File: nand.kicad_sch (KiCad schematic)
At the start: 14 parts, among them U4 MCIMX6Y2DVM09AB, U7 MT29F4G08ABAEAH4

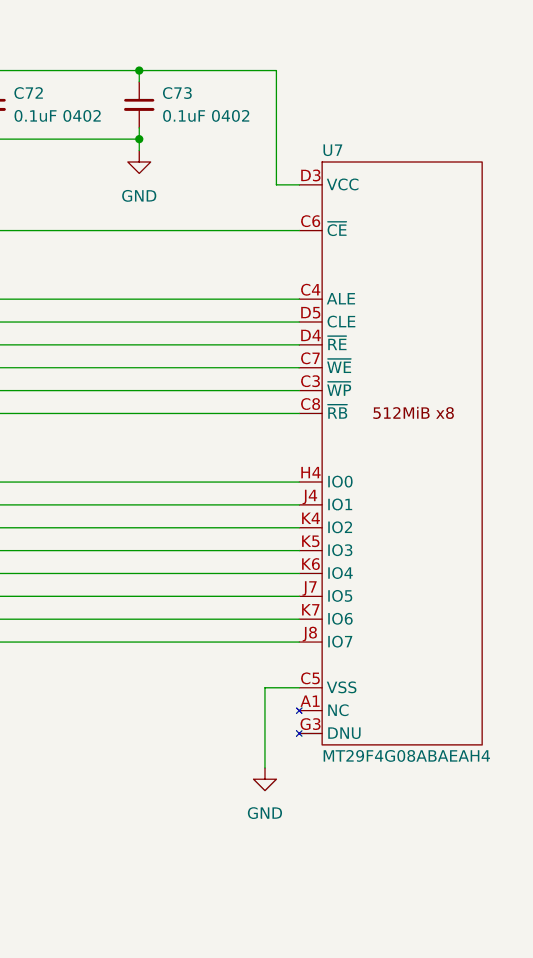
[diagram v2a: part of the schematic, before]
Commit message: Fix NAND and RClamp3374N footprints; ERC
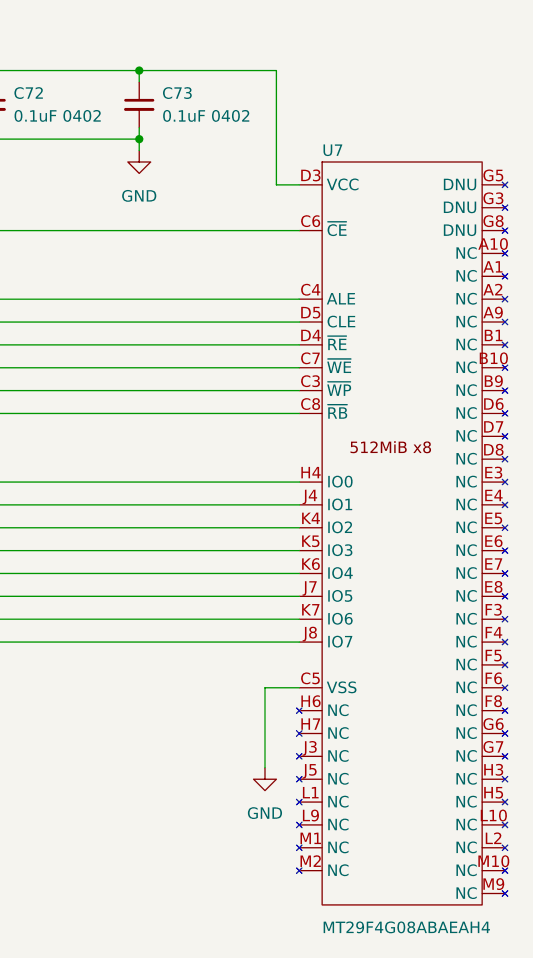
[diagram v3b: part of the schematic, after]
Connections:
- net VCC renamed VDD_3V3
- now unconnected: U7.A1 (NC), U7.A10 (NC), U7.A2 (NC), U7.A9 (NC), U7.B1 (NC), U7.B10 (NC), U7.B9 (NC), U7.D6 (NC), U7.D7 (NC), U7.D8 (NC), U7.E3 (NC), U7.E4 (NC), U7.E5 (NC), U7.E6 (NC), U7.E7 (NC), U7.E8 (NC), U7.F3 (NC), U7.F4 (NC), U7.F5 (NC), U7.F6 (NC), U7.F8 (NC), U7.G3 (DNU), U7.G5 (DNU), U7.G6 (NC), U7.G7 (NC), U7.G8 (DNU), U7.H3 (NC), U7.H5 (NC), U7.H6 (NC), U7.H7 (NC), U7.J3 (NC), U7.J5 (NC), U7.L1 (NC), U7.L10 (NC), U7.L2 (NC), U7.L9 (NC), U7.M1 (NC), U7.M10 (NC), U7.M2 (NC), U7.M9 (NC)
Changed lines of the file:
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@@
       (effects (font (size 1.27 1.27)) (justify left))
     )
-    (property "Value" "MT29F4G08ABAEAH4" (id 1) (at 230.505 135.255 0)
+    (property "Value" "MT29F4G08ABAEAH4" (id 1) (at 230.505 154.305 0)
       (effects (font (size 1.27 1.27)) (justify left))
     )

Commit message: Footprint assignments for standard passives
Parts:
- C67, C68, C70, C71, C72, C73: footprint (none) -> Capacitor_SMD:C_0402_1005Metric
- C69: footprint (none) -> Capacitor_SMD:C_0603_1608Metric
- R22, R23, R24, R25, R26: footprint (none) -> Resistor_SMD:R_0402_1005Metric
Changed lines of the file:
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@@
       (effects (font (size 1.27 1.27)) (justify left))
     )
-    (property "Footprint" "" (id 2) (at 113.665 133.985 0)
+    (property "Footprint" "Capacitor_SMD:C_0402_1005Metric" (id 2) (at 113.665 133.985 0)
       (effects (font (size 1.27 1.27)) hide)
     )
@@
       (effects (font (size 1.27 1.27)) (justify left))
     )
-    (property "Footprint" "" (id 2) (at 210.185 62.865 0)
+    (property "Footprint" "Capacitor_SMD:C_0402_1005Metric" (id 2) (at 210.185 62.865 0)
       (effects (font (size 1.27 1.27)) hide)
     )
@@
       (effects (font (size 1.27 1.27)) (justify left))
     )
-    (property "Footprint" "" (id 2) (at 27.94 81.915 0)
+    (property "Footprint" "Capacitor_SMD:C_0402_1005Metric" (id 2) (at 27.94 81.915 0)
       (effects (font (size 1.27 1.27)) hide)
     )
@@
       (effects (font (size 1.27 1.27)) (justify left))
     )
-    (property "Footprint" "" (id 2) (at 193.675 62.865 0)
+    (property "Footprint" "Capacitor_SMD:C_0402_1005Metric" (id 2) (at 193.675 62.865 0)
       (effects (font (size 1.27 1.27)) hide)
     )
@@
       (effects (font (size 1.27 1.27)) (justify left))
     )
-    (property "Footprint" "" (id 2) (at 118.745 71.755 0)
+    (property "Footprint" "Resistor_SMD:R_0402_1005Metric" (id 2) (at 118.745 71.755 0)
       (effects (font (size 1.27 1.27)) hide)
     )
@@
       (effects (font (size 1.27 1.27)) (justify left))
     )
-    (property "Footprint" "" (id 2) (at 144.145 62.865 0)
+    (property "Footprint" "Capacitor_SMD:C_0603_1608Metric" (id 2) (at 144.145 62.865 0)
       (effects (font (size 1.27 1.27)) hide)
     )
@@
       (effects (font (size 0.8 0.8)))
     )
-    (property "Footprint" "" (id 2) (at 94.615 92.075 0)
+    (property "Footprint" "Resistor_SMD:R_0402_1005Metric" (id 2) (at 94.615 92.075 0)
       (effects (font (size 1.27 1.27)) hide)
     )
@@
       (effects (font (size 0.8 0.8)))
     )
-    (property "Footprint" "" (id 2) (at 94.615 89.535 0)
+    (property "Footprint" "Resistor_SMD:R_0402_1005Metric" (id 2) (at 94.615 89.535 0)
       (effects (font (size 1.27 1.27)) hide)
     )
@@
       (effects (font (size 1.27 1.27)) (justify left))
     )
-    (property "Footprint" "" (id 2) (at 177.165 62.865 0)
+    (property "Footprint" "Capacitor_SMD:C_0402_1005Metric" (id 2) (at 177.165 62.865 0)
       (effects (font (size 1.27 1.27)) hide)
     )
@@
       (effects (font (size 1.27 1.27)) (justify left))
     )
-    (property "Footprint" "" (id 2) (at 160.655 62.865 0)
+    (property "Footprint" "Capacitor_SMD:C_0402_1005Metric" (id 2) (at 160.655 62.865 0)
       (effects (font (size 1.27 1.27)) hide)
     )
@@
       (effects (font (size 1.27 1.27)) (justify left))
     )
-    (property "Footprint" "" (id 2) (at 104.775 71.755 0)
+    (property "Footprint" "Resistor_SMD:R_0402_1005Metric" (id 2) (at 104.775 71.755 0)
       (effects (font (size 1.27 1.27)) hide)
     )
@@
       (effects (font (size 0.8 0.8)))
     )
-    (property "Footprint" "" (id 2) (at 94.615 84.455 0)
-      (effects (font (size 1.27 1.27)) hide)
-    )
+    (property "Footprint" "Resistor_SMD:R_0402_1005Metric" (id 2) (at 94.615 84.455 0)
+      (effects (font (size 1.27 1.27)) hide)
+    )
